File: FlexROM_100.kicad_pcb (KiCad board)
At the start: 2 copper layers, 16.4 x 34.2 mm, 5 parts, among them J1 LH535618 DIP LEGS, U1 28C256

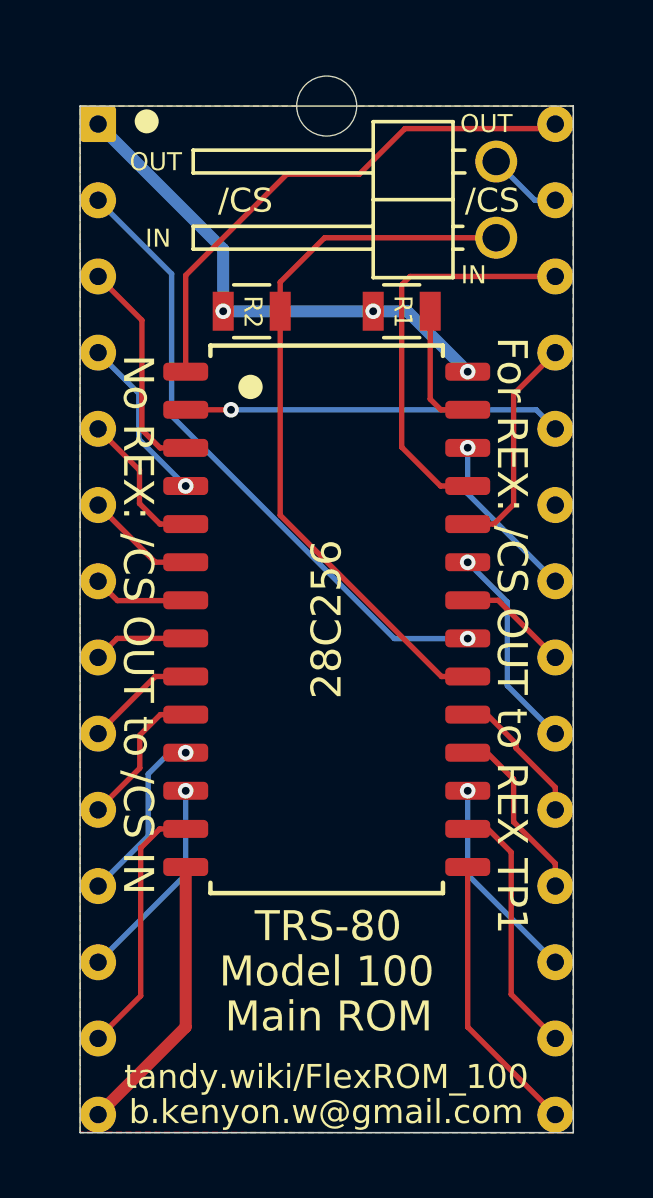
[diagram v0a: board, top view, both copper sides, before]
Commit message: FlexROM_100 programming adapter, FlexROM_102 programming jumpers
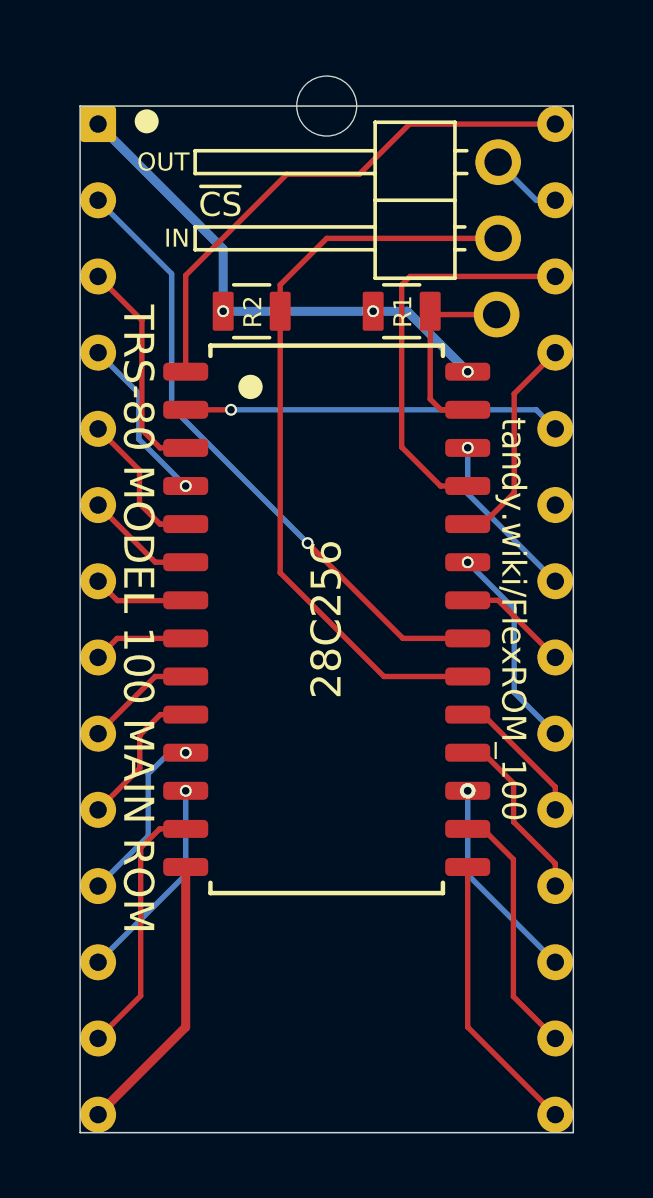
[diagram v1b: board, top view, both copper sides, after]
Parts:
- added J2: ~WE~, 000_LOCAL:Pin_1x1_hole, F.Cu at (155.7, 89.8)
- J1: footprint 000_LOCAL:DIP-28_W15.24mm_pcb_sil_pins -> 000_LOCAL:DIP28_0.6_pcb_sil_pins
- JP1: value /CS breakout (REX TP1) -> ~CS~ breakout (REX TP1)
- moved JP1 0.07 mm to (155.7, 87.3)
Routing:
- net /~WE: track 4.33 -> 6.59 mm
- net /~CS_IN: track 24.1 -> 25.2 mm
- removed copper zone on B.Cu, net /GND
- removed copper zone on F.Cu, net /GND
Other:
- net class Default: clearance 0.2 -> 0.16; trace_width 0.25 -> 0.18; via_dia 0.8 -> 0.4; via_drill 0.4 -> 0.25
- rule trace_clearance: 0.2 -> 0.16
- rule via_min_drill: 0.26 -> 0.25
- rule via_min_size: 0.52 -> 0.4
- board text added: "Connect ~CS~ OUT to REX TP1. Leave ~CS~ IN unconnected."
- board text added: "If REX is later removed, connect ~CS~ OUT to ~CS~ IN."
- board text added: "Install a shunt on ~CS~, or, install wires as above,"
- board text added: "Run 2 wires from ~CS~ IN & ~CS~ OUT to Option ROM compartment."
- board text added: "TRS-80 MODEL 100 MAIN ROM"
- board text added: "~CS"
- board text removed: "/CS"
- board text removed: "Connect /CS OUT to REX TP1. Leave /CS IN unconnected."
- board text removed: "For REX: /CS OUT to REX TP1"
- board text removed: "If REX is later removed, connect /CS OUT to /CS IN."
- board text removed: "Install a shunt on /CS, or, install wires as above,"
- board text removed: "Main ROM"
- board text removed: "Model 100"
- board text removed: "No REX: /CS OUT to /CS IN"
- board text removed: "Run 2 wires from /CS IN & /CS OUT to Option ROM compartment."
- board text removed: "TRS-80"
- board text removed: "b.kenyon.w@gmail.com"

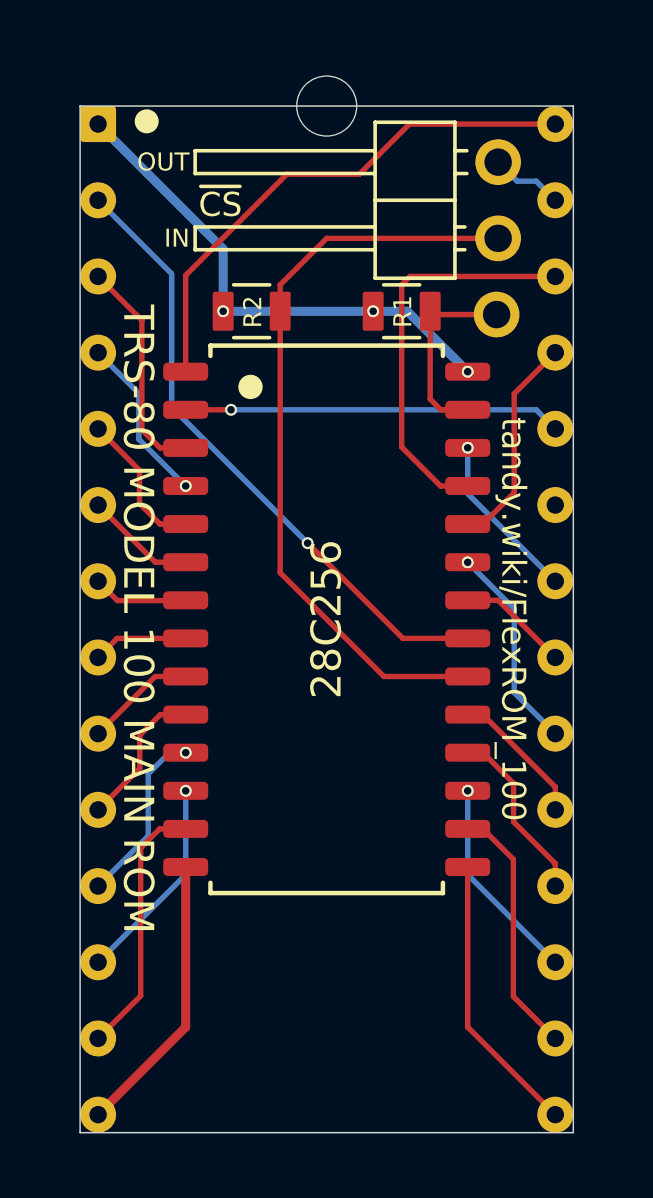
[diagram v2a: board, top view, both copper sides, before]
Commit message: Add FlashROM_100. /WE pin on FlexROM_100
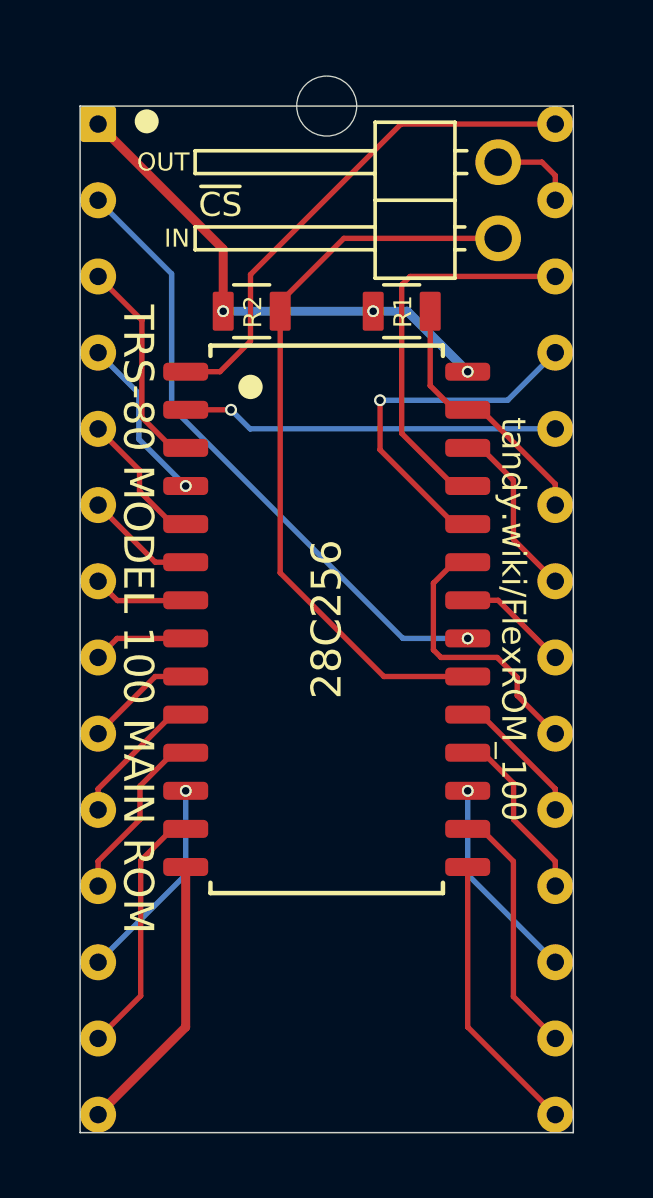
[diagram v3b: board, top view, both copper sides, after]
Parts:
- removed J2: ~WE~, 000_LOCAL:Pin_1x1_hole
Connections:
- J1 pad 23: (no net) -> /~WE
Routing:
- net /A9: track 7.22 -> 12.6 mm, vias 0 -> 1
- net /A11: track 6.92 -> 9.23 mm, vias 1 -> 0
- net /~WE: track 6.59 -> 8.86 mm
- net /A14: track 17.6 -> 17.0 mm
- net /A13: track 5.66 -> 5.91 mm, vias 1 -> 0
- net /D0: track 5.97 -> 5.90 mm, vias 1 -> 0

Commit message: minor touches
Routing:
- net /~CS_IN: track 24.9 -> 23.8 mm
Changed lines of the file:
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@@
   (segment (start 142.38 108.89) (end 142.38 108.0645) (width 0.18) (layer F.Cu) (net 20))
   (segment (start 154.7 96.825) (end 155.207 96.825) (width 0.18) (layer F.Cu) (net 21))
-  (segment (start 156.0325 92.6975) (end 157.62 91.11) (width 0.18) (layer B.Cu) (net 21))
-  (segment (start 151.778 92.6975) (end 156.0325 92.6975) (width 0.18) (layer B.Cu) (net 21))
   (segment (start 154.2545 96.825) (end 154.7 96.825) (width 0.18) (layer F.Cu) (net 21))
   (segment (start 151.778 94.3485) (end 154.2545 96.825) (width 0.18) (layer F.Cu) (net 21))
   (segment (start 151.778 92.6975) (end 151.778 94.3485) (width 0.18) (layer F.Cu) (net 21))
   (via (at 151.778 92.6975) (size 0.4) (drill 0.25) (layers F.Cu B.Cu) (net 21))
+  (segment (start 151.778 92.6975) (end 156.0325 92.6975) (width 0.18) (layer B.Cu) (net 21))
+  (segment (start 156.0325 92.6975) (end 157.62 91.11) (width 0.18) (layer B.Cu) (net 21))
   (segment (start 145.3 105.715) (end 145.3 105.715) (width 0.18) (layer F.Cu) (net 22))
   (via (at 145.3 105.715) (size 0.4) (drill 0.25) (layers F.Cu B.Cu) (net 22))
@@
   (segment (start 144.8565 106.985) (end 143.8 108.0415) (width 0.18) (layer F.Cu) (net 24))
   (segment (start 145.3 106.985) (end 144.8565 106.985) (width 0.18) (layer F.Cu) (net 24))
+  (segment (start 155.715 84.76) (end 157.1755 84.76) (width 0.18) (layer F.Cu) (net 25))
+  (segment (start 157.1755 84.76) (end 157.62 85.2045) (width 0.18) (layer F.Cu) (net 25))
   (segment (start 157.62 85.2045) (end 157.62 86.03) (width 0.18) (layer F.Cu) (net 25))
-  (segment (start 157.1755 84.76) (end 157.62 85.2045) (width 0.18) (layer F.Cu) (net 25))
-  (segment (start 155.715 84.76) (end 157.1755 84.76) (width 0.18) (layer F.Cu) (net 25))
   (segment (start 145.3 113.59) (end 142.38 116.51) (width 0.3) (layer F.Cu) (net 26))
   (segment (start 145.3 108.255) (end 145.3 113.59) (width 0.3) (layer F.Cu) (net 26))
-  (segment (start 152.4765 83.49) (end 157.62 83.49) (width 0.18) (layer F.Cu) (net 27))
-  (segment (start 147.46 88.5065) (end 152.4765 83.49) (width 0.18) (layer F.Cu) (net 27))
-  (segment (start 147.46 90.729) (end 147.46 88.5065) (width 0.18) (layer F.Cu) (net 27))
+  (segment (start 152.76 83.49) (end 157.62 83.49) (width 0.18) (layer F.Cu) (net 27))
+  (segment (start 147.46 88.79) (end 152.76 83.49) (width 0.18) (layer F.Cu) (net 27))
+  (segment (start 147.46 90.729) (end 147.46 88.79) (width 0.18) (layer F.Cu) (net 27))
   (segment (start 146.444 91.745) (end 147.46 90.729) (width 0.18) (layer F.Cu) (net 27))
   (segment (start 145.3 91.745) (end 146.444 91.745) (width 0.18) (layer F.Cu) (net 27))
-  (segment (start 151.905 101.905) (end 154.7 101.905) (width 0.18) (layer F.Cu) (net 28))
-  (segment (start 148.45 98.45) (end 151.905 101.905) (width 0.18) (layer F.Cu) (net 28))
-  (segment (start 148.45 89.73) (end 148.45 98.45) (width 0.18) (layer F.Cu) (net 28))
   (segment (start 148.45 89.4215) (end 148.45 89.73) (width 0.18) (layer F.Cu) (net 28))
   (segment (start 150.5715 87.3) (end 148.45 89.4215) (width 0.18) (layer F.Cu) (net 28))
   (segment (start 155.715 87.3) (end 150.5715 87.3) (width 0.18) (layer F.Cu) (net 28))
+  (segment (start 153.755 101.905) (end 154.7 101.905) (width 0.18) (layer F.Cu) (net 28))
+  (segment (start 148.45 96.6) (end 153.755 101.905) (width 0.18) (layer F.Cu) (net 28))
+  (segment (start 148.45 89.73) (end 148.45 96.6) (width 0.18) (layer F.Cu) (net 28))
   (segment (start 153.56 89.84) (end 153.45 89.73) (width 0.18) (layer F.Cu) (net 29))
   (segment (start 155.1435 93.015) (end 154.7 93.015) (width 0.18) (layer F.Cu) (net 29))

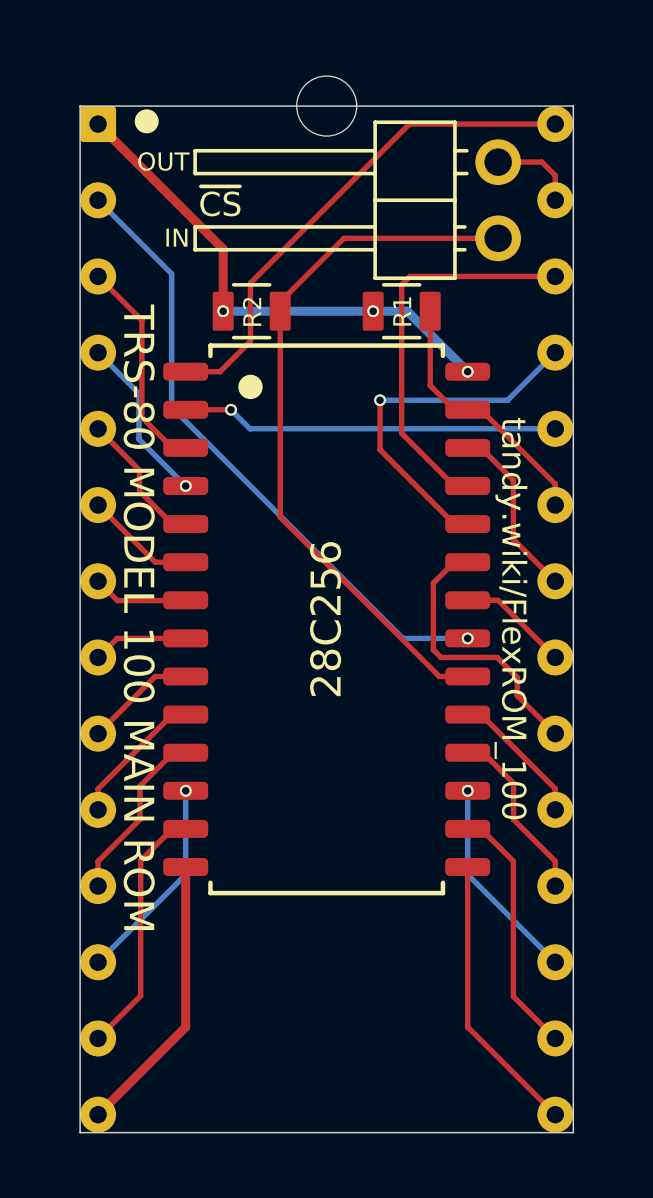
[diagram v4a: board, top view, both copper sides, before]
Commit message: FlexROM_100 & FlashROM_100 fix ALE/WE
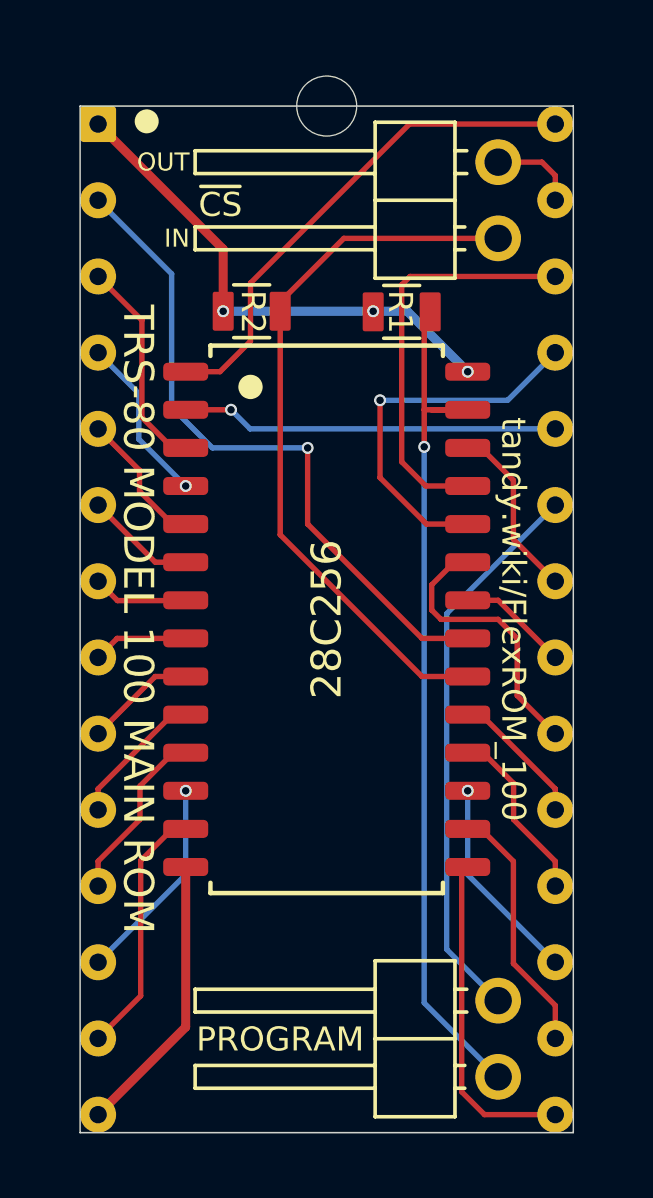
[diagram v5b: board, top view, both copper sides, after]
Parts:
- added JP2: PROGRAM, 000_LOCAL:Pin_Header_Angled_1x02_Pitch2.54mm, F.Cu at (155.7, 115.2)
- JP1: value ~CS~ breakout (REX TP1) -> ~CS~ breakout
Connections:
- J1 pad 23: /~WE -> /ALE
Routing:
- net /~WE: track 8.86 -> 28.8 mm, vias 0 -> 1
- net /ALE: track 0.00 -> 18.7 mm
- net /D3: track 9.46 -> 11.0 mm
- net /A10: track 21.0 -> 22.5 mm
- net /A8: track 13.1 -> 13.7 mm
- net /A9: track 12.6 -> 13.1 mm
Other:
- board text added: "PROGRAM"

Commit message: simpler programming adapters, update pics and BOMs
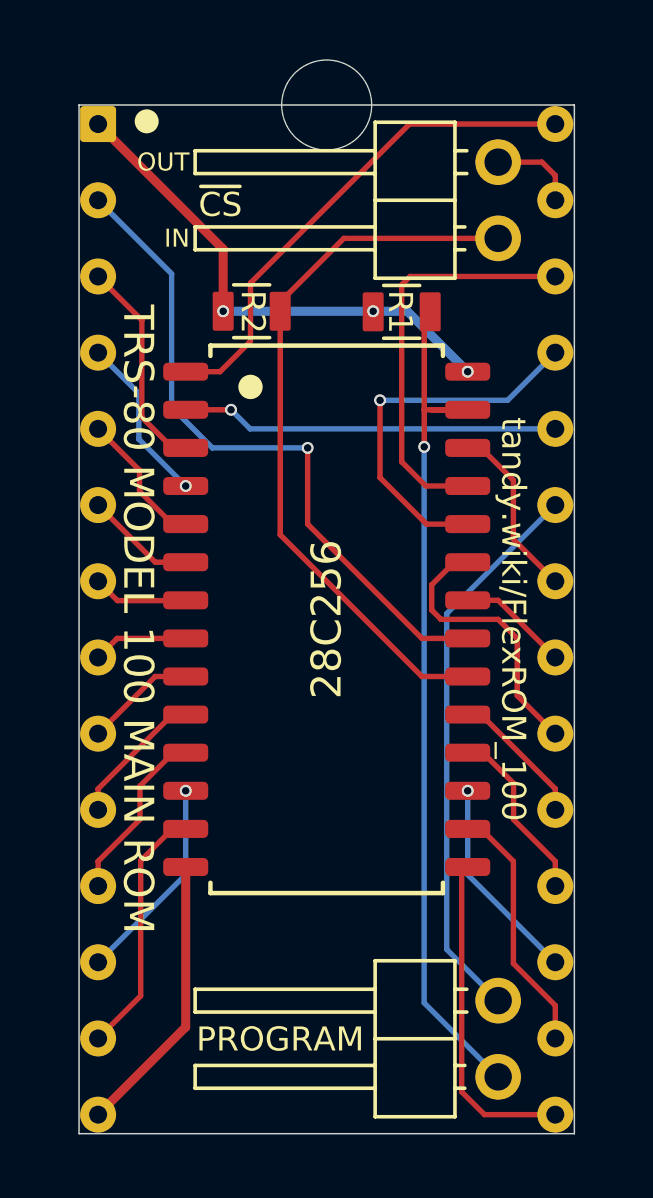
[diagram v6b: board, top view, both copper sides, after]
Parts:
- added REF**: NPTH_3mm, 000_LOCAL:NPTH_3mm, F.Cu at (150.0, 82.9)
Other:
- board size 16.4 x 34.2 mm -> 16.5 x 34.3 mm

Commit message: add FlashROM_100_tsop
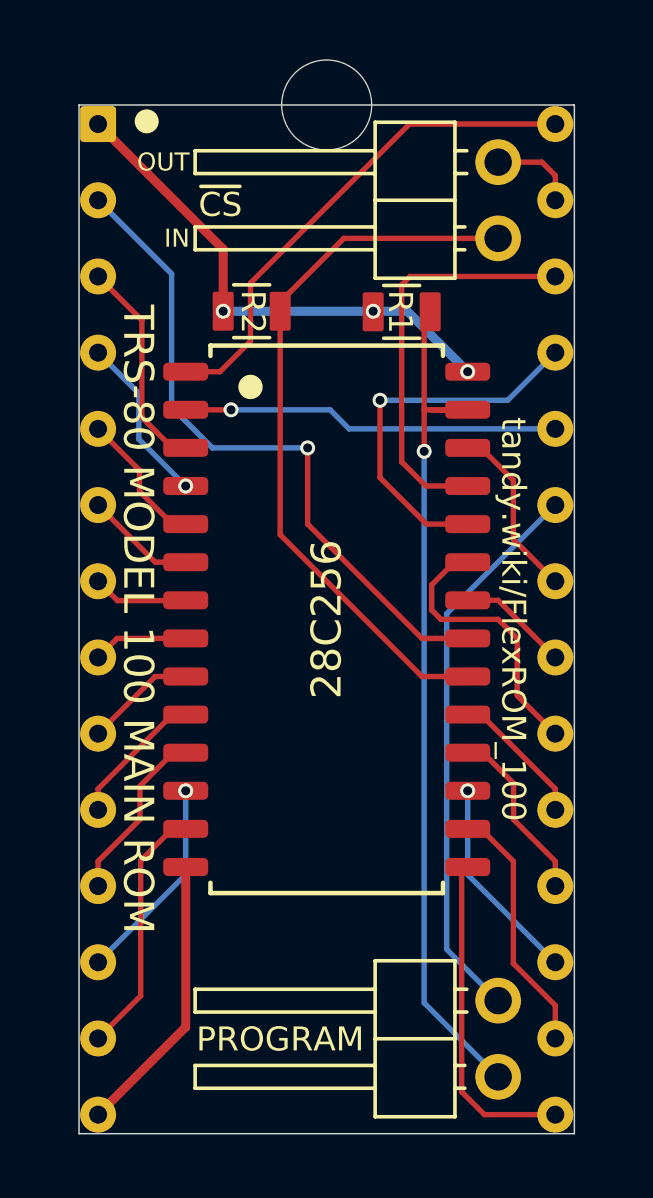
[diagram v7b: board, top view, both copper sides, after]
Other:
- net class Default: via_dia 0.4 -> 0.5; via_drill 0.25 -> 0.3
- rule via_min_drill: 0.25 -> 0.3
- rule via_min_size: 0.4 -> 0.5

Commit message: add model 100 optrom programming adapter. readme and renders
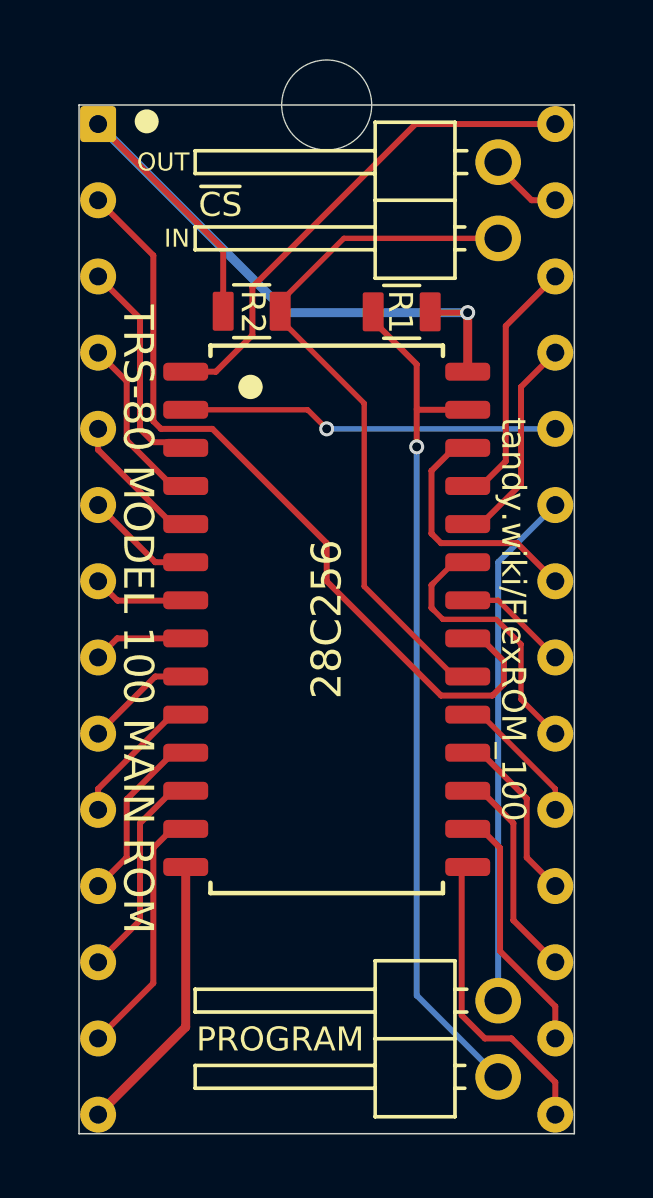
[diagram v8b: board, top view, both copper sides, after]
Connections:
- R1 pad 1: /~WE -> /VCC
- R1 pad 2: /VCC -> /~WE
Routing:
- net /VCC: track 17.0 -> 26.1 mm, vias 3 -> 1
- net /A9: track 13.1 -> 7.18 mm, vias 1 -> 0
- net /A8: track 13.7 -> 8.45 mm
- net /A10: track 22.5 -> 26.8 mm, vias 1 -> 0
- net /A13: track 5.91 -> 8.40 mm
- net /ALE: track 18.7 -> 17.3 mm
- net /D3: track 11.0 -> 10.2 mm
- net /~CS_IN: track 24.1 -> 23.5 mm
- net /A6: track 5.65 -> 5.91 mm, vias 1 -> 0
- net /D5: track 6.92 -> 7.18 mm, vias 1 -> 0
- net /D1: track 6.92 -> 7.18 mm, vias 1 -> 0
